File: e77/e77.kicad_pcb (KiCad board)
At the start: 2 copper layers, 30 x 52 mm, 18 parts, among them J1 Conn_01x06_Pin, J2 Conn_01x06_Pin, U1 XBEE_MODULE, U2 XBEE_MODULE, U3 E77, U4 Rak3172

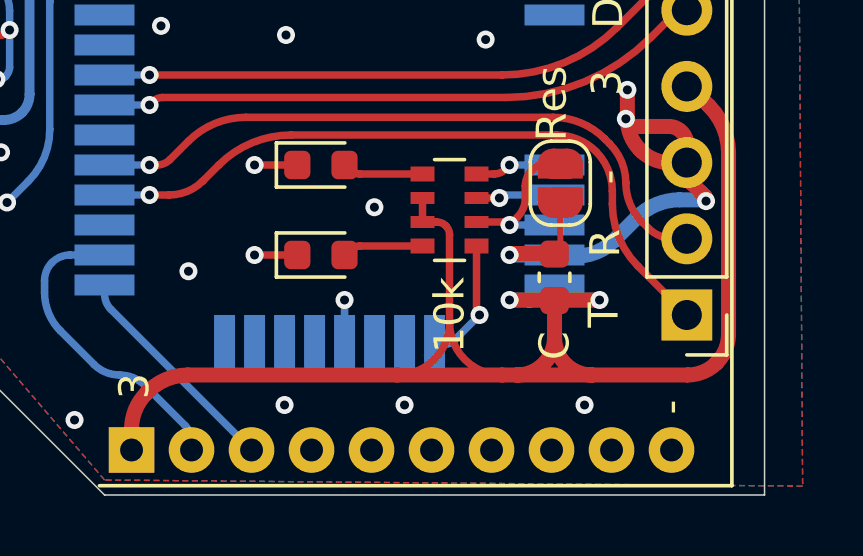
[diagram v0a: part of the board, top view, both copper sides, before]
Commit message: add Radiohead_Lib
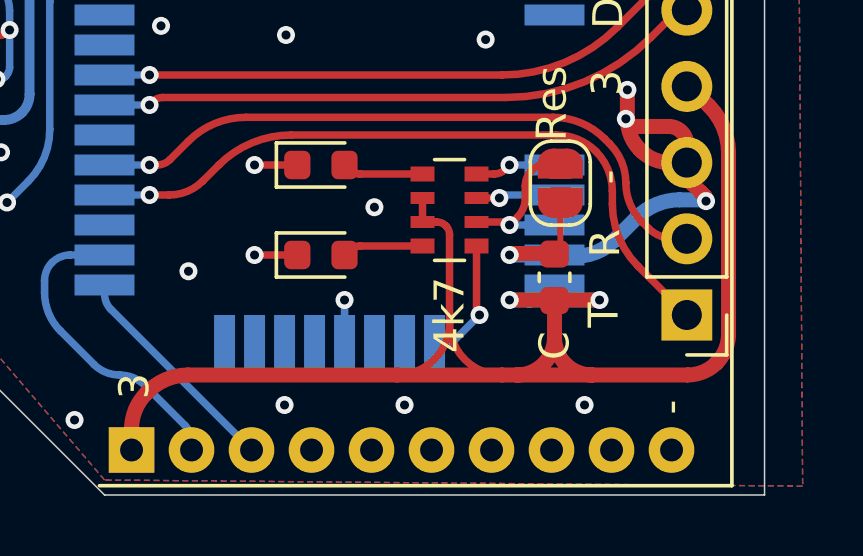
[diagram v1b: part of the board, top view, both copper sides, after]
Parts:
- RN2: value 10k -> 4k7
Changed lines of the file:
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@@
 			)
 		)
-		(property "Value" "10k"
+		(property "Value" "4k7"
 			(at 0 -3.5 -90)
 			(layer "F.SilkS")
